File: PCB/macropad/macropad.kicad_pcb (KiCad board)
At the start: 2 copper layers, 82.5 x 92 mm, 26 parts, among them J1 Conn_01x04, SW1 SW_Push_45deg, SW10 SW_Push_45deg, SW11 SW_Push_45deg, SW12 RotaryEncoder_Switch, SW2 SW_Push_45deg, SW3 SW_Push_45deg, SW4 SW_Push_45deg, SW5 SW_Push_45deg, SW6 SW_Push_45deg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

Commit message: Wired components together on PCB
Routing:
- net Col 2: track 0.00 -> 139.2 mm
- net EC11B: track 0.00 -> 133.9 mm
- net SDA: track 0.00 -> 118.2 mm
- net Row 3: track 0.00 -> 116.1 mm
- net SCL: track 0.00 -> 111.4 mm
- net Col 1: track 0.00 -> 110.1 mm
- net Col 0: track 0.00 -> 98.9 mm
- net Row 2: track 0.00 -> 94.1 mm
- net GND: track 0.00 -> 76.0 mm
- net Row 1: track 0.00 -> 75.9 mm
- net VCC: track 0.00 -> 74.6 mm
- net Row 0: track 0.00 -> 71.1 mm
- net EC11A: track 0.00 -> 48.3 mm
- net Net-(D1-A): track 0.00 -> 14.7 mm
- net Net-(D5-A): track 0.00 -> 14.7 mm
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
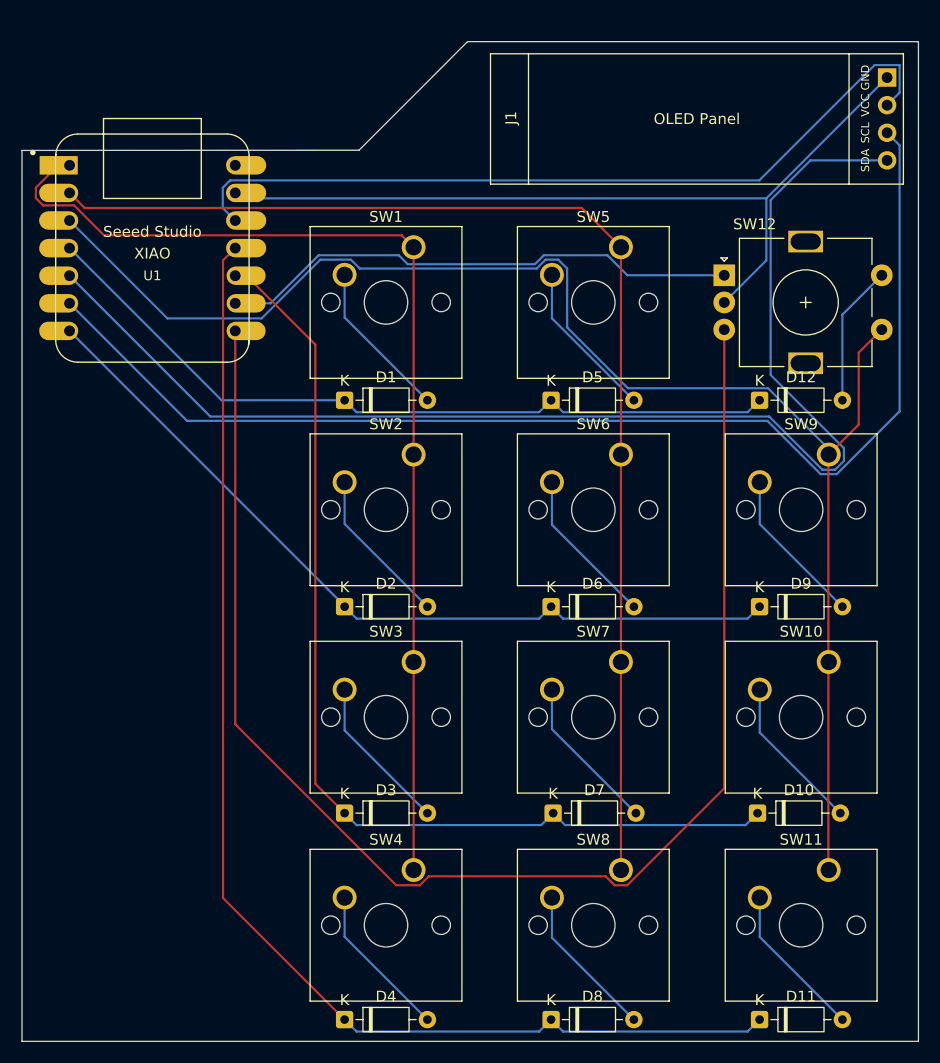
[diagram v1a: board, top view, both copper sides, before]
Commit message: Update macropad PCB: silk, footprint, gerbers
Add fabrication-toolkit-options.json and Production/gerbers.zip. Modify macropad.kicad_pcb to change drillshape to 0 and set CAM outputdirectory to ../../Production/, add a MountingHole_3.2mm_M3 footprint, and regenerate extensive F.SilkS artwork (gr_poly/gr_line/gr_curve elements), edge cuts and board text (author/version/part name). Remove temporary KiCad .lck files and update macropad.kicad_pro accordingly.
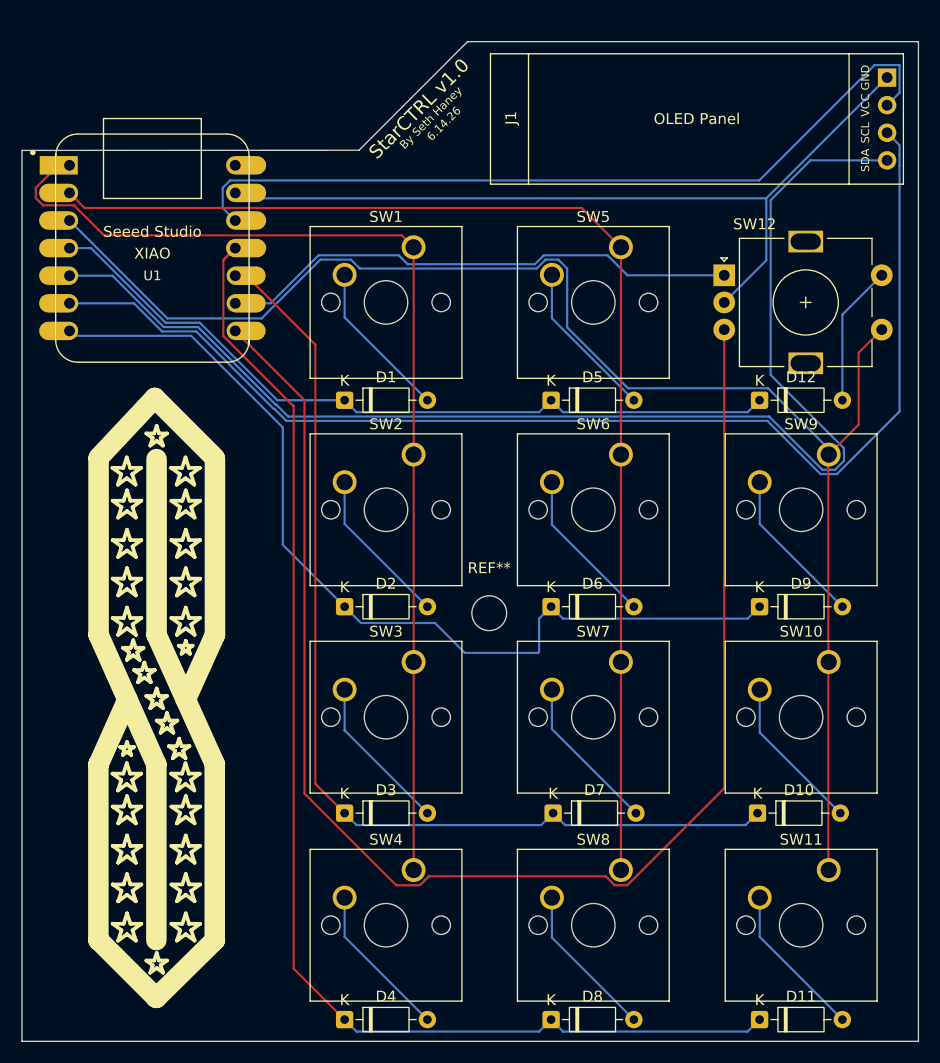
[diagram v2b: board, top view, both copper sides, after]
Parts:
- added REF**: MountingHole_3.2mm_M3, MountingHole:MountingHole_3.2mm_M3, F.Cu at (58.0, 92.6)
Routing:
- net Row 1: track 75.9 -> 86.6 mm
- net Row 3: track 116.1 -> 117.7 mm
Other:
- board text added: "6.14.26"
- board text added: "By Seth Haney"
- board text added: "StarCTRL v1.0"
